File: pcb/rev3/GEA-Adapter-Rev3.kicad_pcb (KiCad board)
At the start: 2 copper layers, 88.7 x 40 mm, 109 parts, among them J1 8P8C, J3 TC2030, J4 USB_C_Receptacle_USB2.0_16P, Q3 CJ3407, Q4 CJ3407, Q5 MMBT3904, SW1 SW_Push, SW2 SW_Push, U10 TPS22810DBVR, U2 ESP32-C3-WROOM-02, U4 74LVC2G07, U5 74LVC2G07_3v3, U6 AP2112K-3.3, U7 USBLC6-2SC6, U8 AP63205WU, U9 TPS22810DBVR

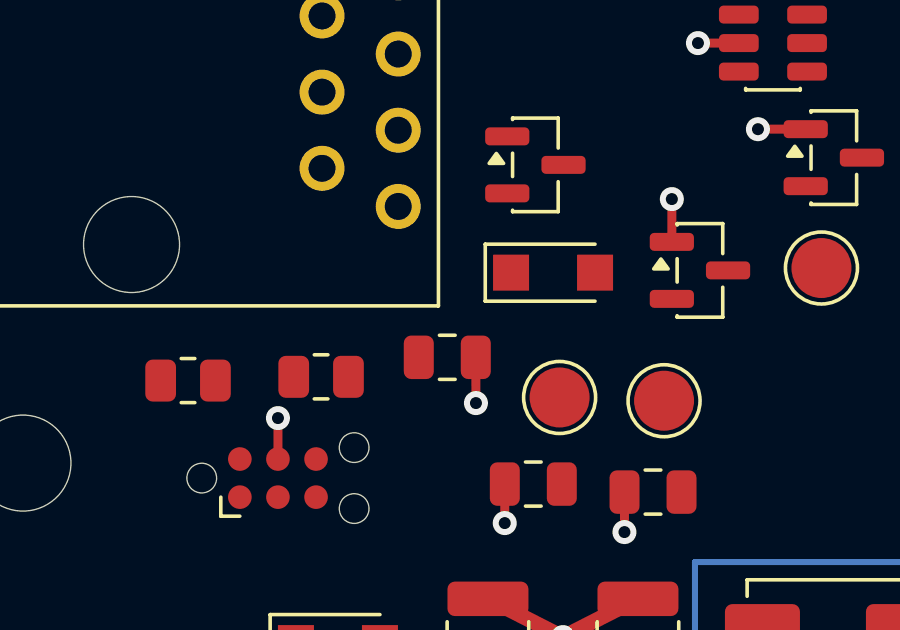
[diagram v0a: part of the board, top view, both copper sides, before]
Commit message: feat(pcb): route rev3a 5v branch
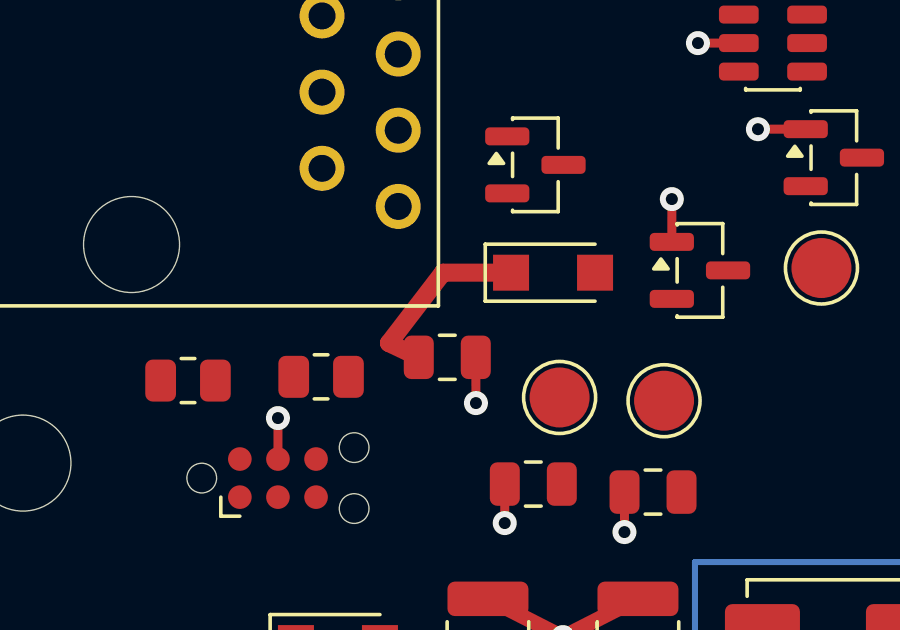
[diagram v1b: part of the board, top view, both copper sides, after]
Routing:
- net +5V: track 0.00 -> 6.33 mm
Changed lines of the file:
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@@
+	)
+	(segment
+		(start 20.270282 23.653262)
+		(end 18 23.653262)
+		(width 0.6)
+		(layer "F.Cu")
+		(net 2)
+	)
+	(segment
+		(start 18 23.653262)
+		(end 16.2 26)
+		(width 0.6)
+		(layer "F.Cu")
+		(net 2)
+	)
+	(segment
+		(start 16.2 26)
+		(end 17.194716 26.474524)
+		(width 0.6)
+		(layer "F.Cu")
+		(net 2)
 	)
 	(segment

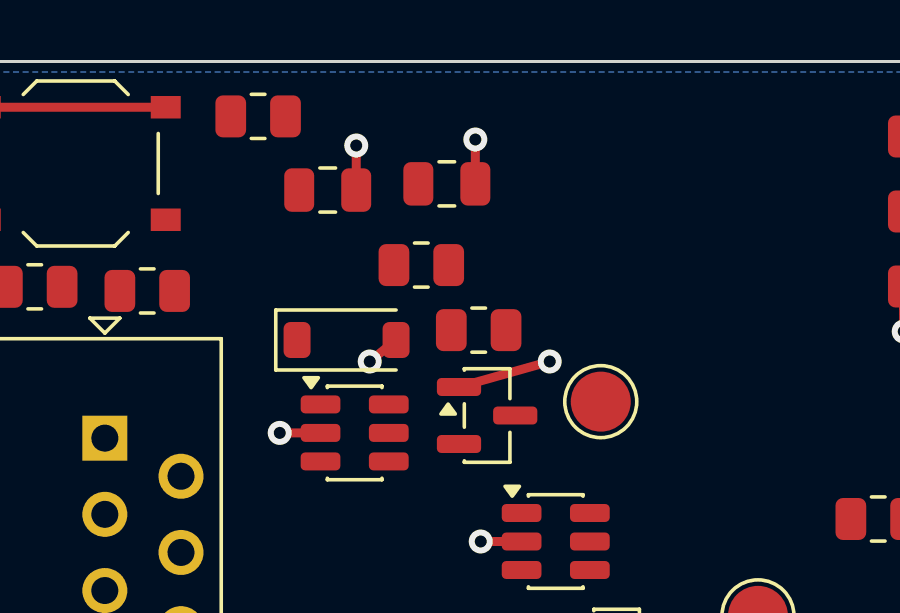
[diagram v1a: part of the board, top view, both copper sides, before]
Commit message: feat(pcb): route rev3a 3v3 branch
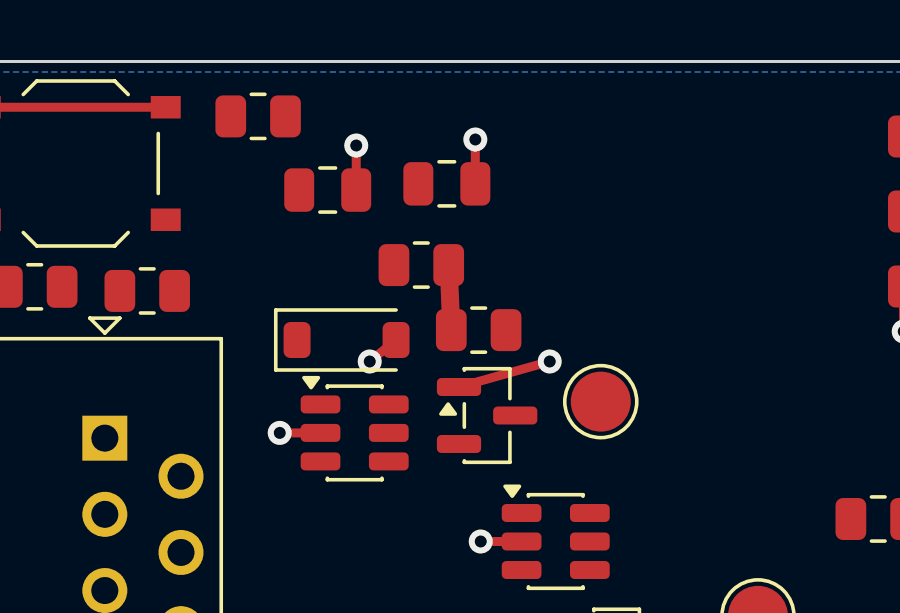
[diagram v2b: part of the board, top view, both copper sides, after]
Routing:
- net +3V3: track 0.00 -> 2.17 mm
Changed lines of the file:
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@@
+	)
+	(segment
+		(start 25.431711 6.786079)
+		(end 25.519272 8.9541)
+		(width 0.6)
+		(layer "F.Cu")
+		(net 1)
 	)
 	(segment

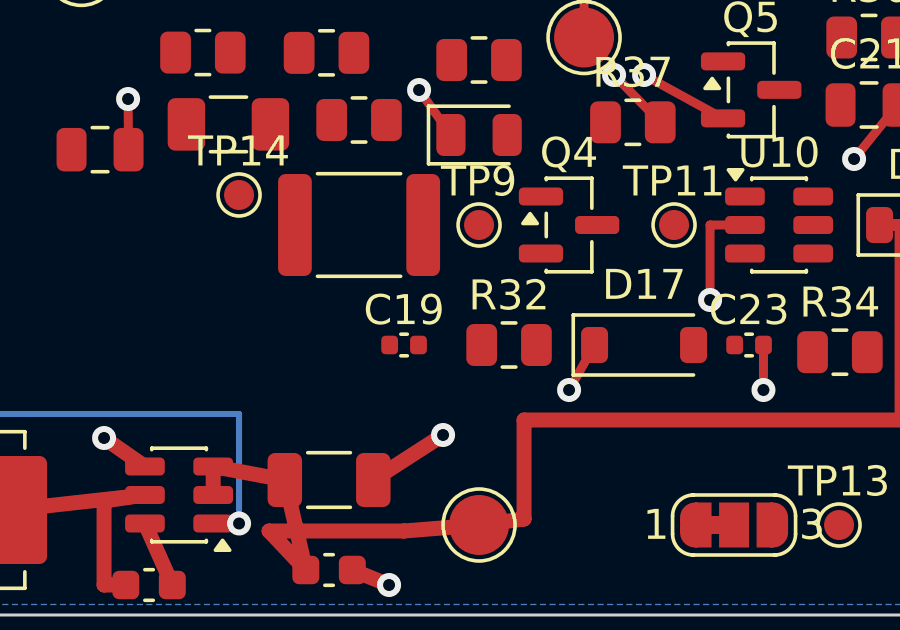
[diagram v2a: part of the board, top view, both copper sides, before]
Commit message: feat(pcb): route rev3a pin3 fused path
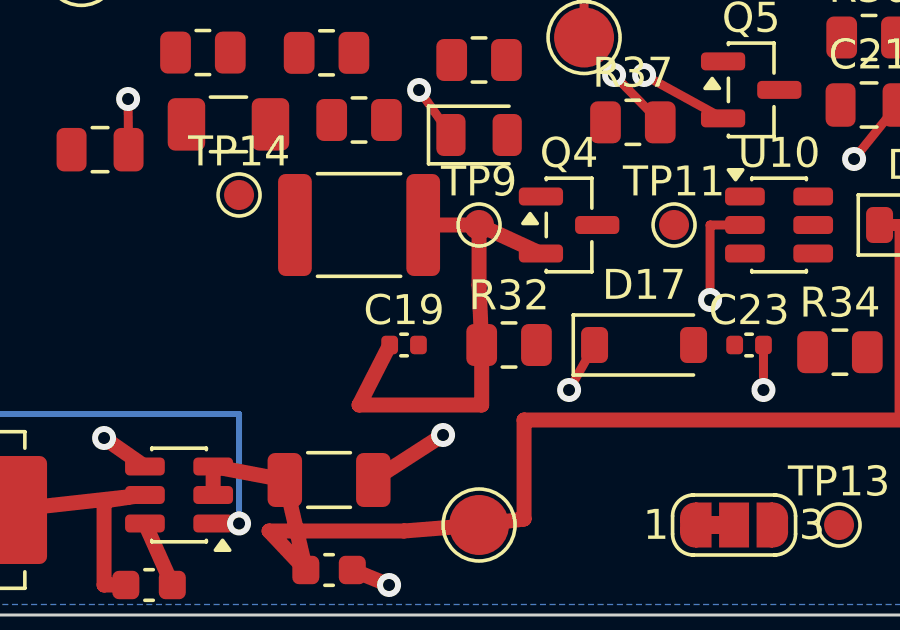
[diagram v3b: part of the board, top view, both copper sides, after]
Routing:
- net PIN3_FUSED: track 0.00 -> 16.5 mm
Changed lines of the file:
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@@
+	)
+	(segment
+		(start 47.1375 27)
+		(end 49 27)
+		(width 0.5)
+		(layer "F.Cu")
+		(net 58)
+	)
+	(segment
+		(start 49.0875 33)
+		(end 49.0875 31)
+		(width 0.5)
+		(layer "F.Cu")
+		(net 58)
+	)
+	(segment
+		(start 46.02 31)
+		(end 45 33)
+		(width 0.5)
+		(layer "F.Cu")
+		(net 58)
+	)
+	(segment
+		(start 49 27)
+		(end 51.0625 27.95)
+		(width 0.5)
+		(layer "F.Cu")
+		(net 58)
+	)
+	(segment
+		(start 45 33)
+		(end 49.0875 33)
+		(width 0.5)
+		(layer "F.Cu")
+		(net 58)
+	)
+	(segment
+		(start 49.0875 31)
+		(end 49 29)
+		(width 0.5)
+		(layer "F.Cu")
+		(net 58)
+	)
+	(segment
+		(start 49 29)
+		(end 49 27)
+		(width 0.5)
+		(layer "F.Cu")
+		(net 58)
 	)
 	(segment

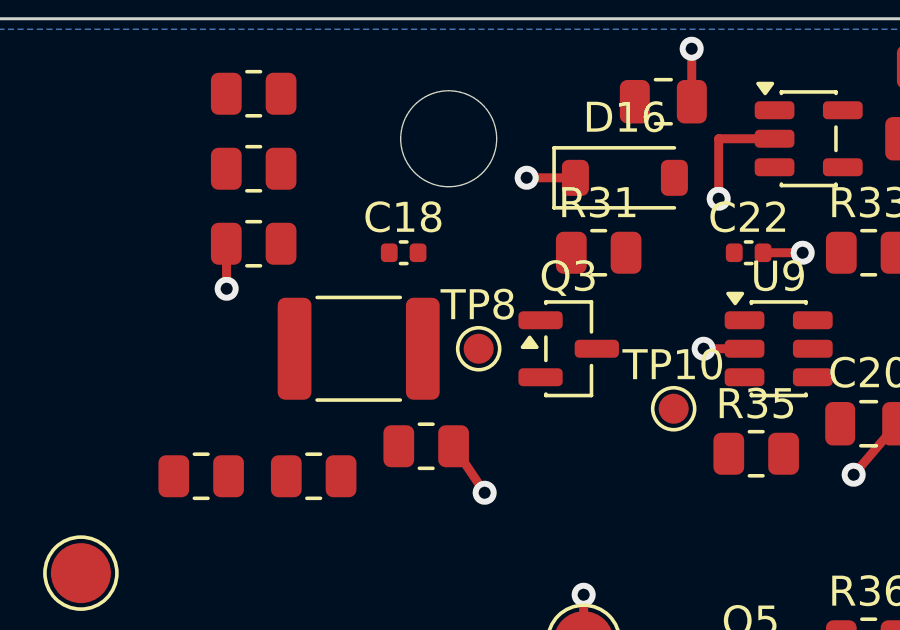
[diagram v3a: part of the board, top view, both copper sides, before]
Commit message: feat(pcb): route rev3a pin1 fused path
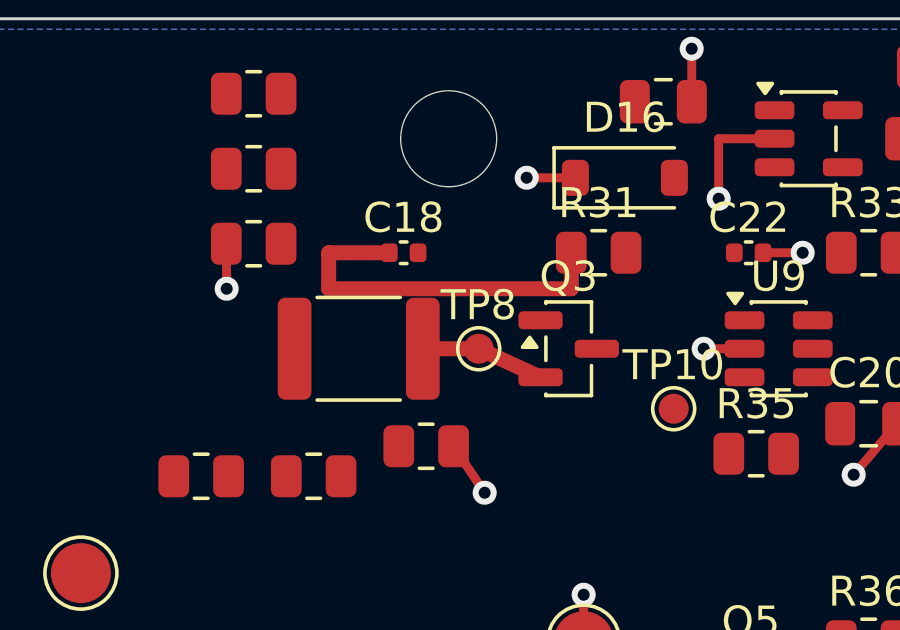
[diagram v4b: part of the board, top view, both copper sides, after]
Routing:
- net PIN1_FUSED: track 0.00 -> 16.6 mm
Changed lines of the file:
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@@
+	)
+	(segment
+		(start 46.02 7.8)
+		(end 44 7.8)
+		(width 0.5)
+		(layer "F.Cu")
+		(net 45)
+	)
+	(segment
+		(start 44 9)
+		(end 52.0875 9)
+		(width 0.5)
+		(layer "F.Cu")
+		(net 45)
+	)
+	(segment
+		(start 44 7.8)
+		(end 44 9)
+		(width 0.5)
+		(layer "F.Cu")
+		(net 45)
+	)
+	(segment
+		(start 52.0875 9)
+		(end 52.0875 7.8)
+		(width 0.5)
+		(layer "F.Cu")
+		(net 45)
+	)
+	(segment
+		(start 47.1375 11)
+		(end 49 11)
+		(width 0.5)
+		(layer "F.Cu")
+		(net 45)
+	)
+	(segment
+		(start 49 11)
+		(end 51.0625 11.95)
+		(width 0.5)
+		(layer "F.Cu")
+		(net 45)
 	)
 	(segment

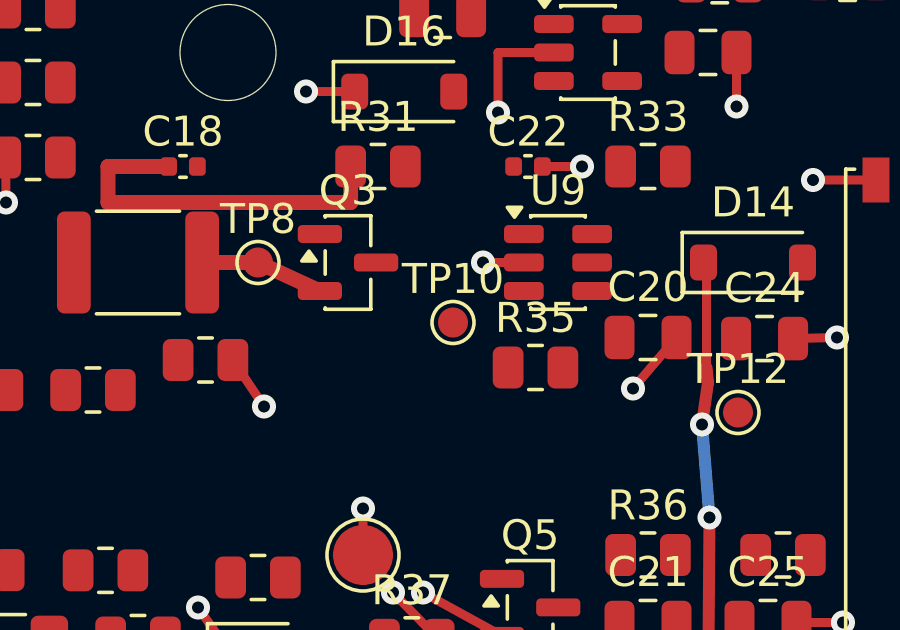
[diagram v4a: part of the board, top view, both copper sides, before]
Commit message: feat(pcb): route rev3a pin1 protected path
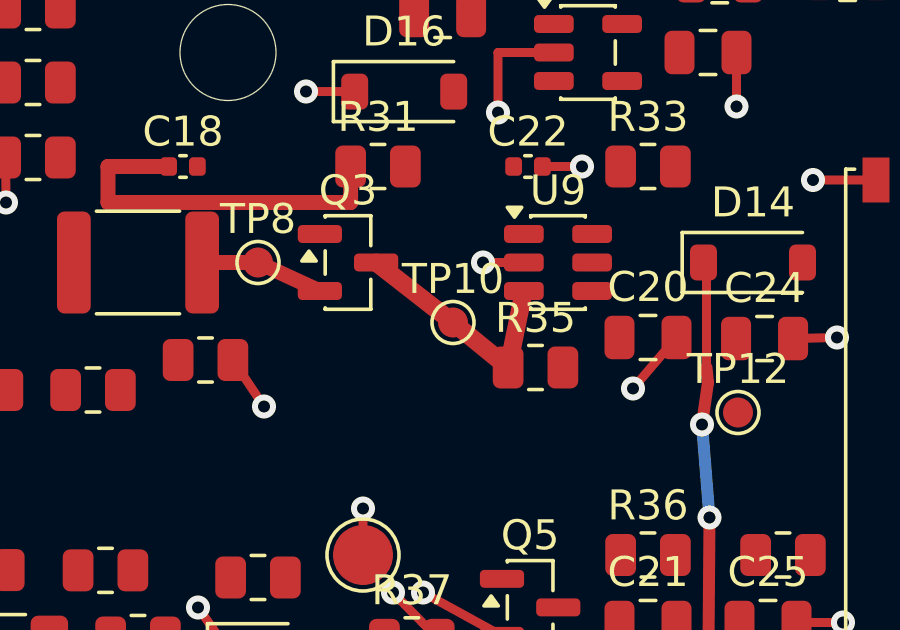
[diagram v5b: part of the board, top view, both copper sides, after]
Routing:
- net PIN1_PROTECTED: track 0.00 -> 8.23 mm
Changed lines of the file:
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@@
+	)
+	(segment
+		(start 52.9375 11)
+		(end 55.5 13)
+		(width 0.6)
+		(layer "F.Cu")
+		(net 42)
+	)
+	(segment
+		(start 57.8625 11.95)
+		(end 57.3375 14.5)
+		(width 0.6)
+		(layer "F.Cu")
+		(net 42)
+	)
+	(segment
+		(start 55.5 13)
+		(end 57.3375 14.5)
+		(width 0.6)
+		(layer "F.Cu")
+		(net 42)
 	)
 	(segment

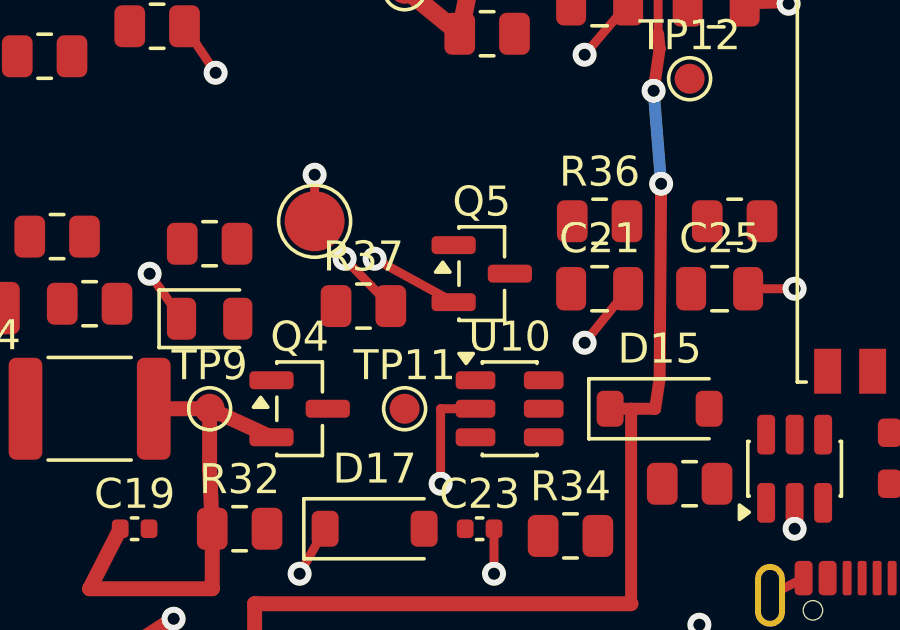
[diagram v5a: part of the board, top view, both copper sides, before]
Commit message: feat(pcb): route rev3a pin3 protected path
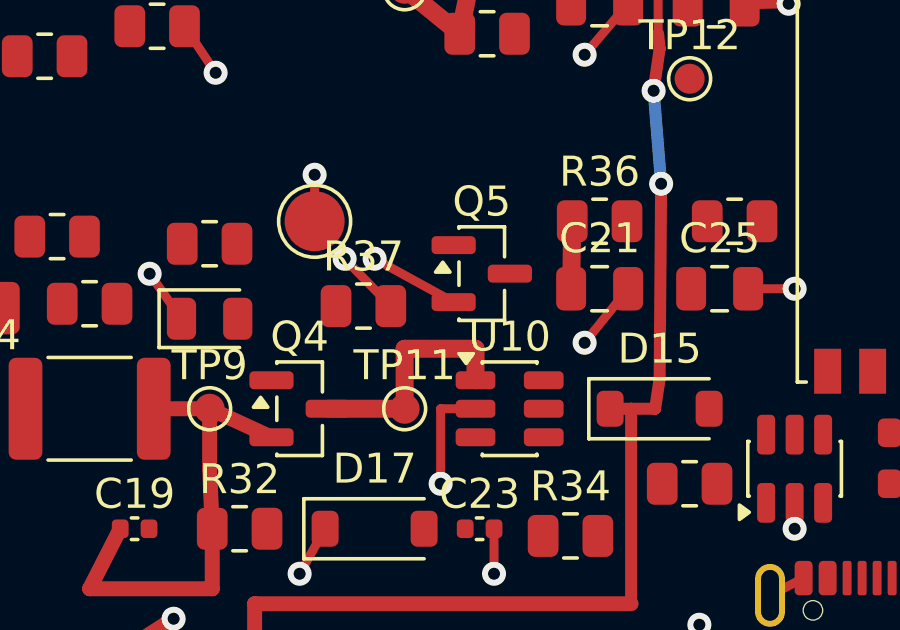
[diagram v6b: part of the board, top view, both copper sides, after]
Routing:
- net PIN3_PROTECTED: track 0.00 -> 10.2 mm
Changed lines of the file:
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@@
+	)
+	(segment
+		(start 61.0875 20.75)
+		(end 61.05 23)
+		(width 0.6)
+		(layer "F.Cu")
+		(net 59)
+	)
+	(segment
+		(start 55.5 27)
+		(end 55.5 25)
+		(width 0.6)
+		(layer "F.Cu")
+		(net 59)
+	)
+	(segment
+		(start 52.9375 27)
+		(end 55.5 27)
+		(width 0.6)
+		(layer "F.Cu")
+		(net 59)
+	)
+	(segment
+		(start 57.8625 25)
+		(end 57.8625 26.05)
+		(width 0.6)
+		(layer "F.Cu")
+		(net 59)
+	)
+	(segment
+		(start 55.5 25)
+		(end 57.8625 25)
+		(width 0.6)
+		(layer "F.Cu")
+		(net 59)
 	)
 	(segment

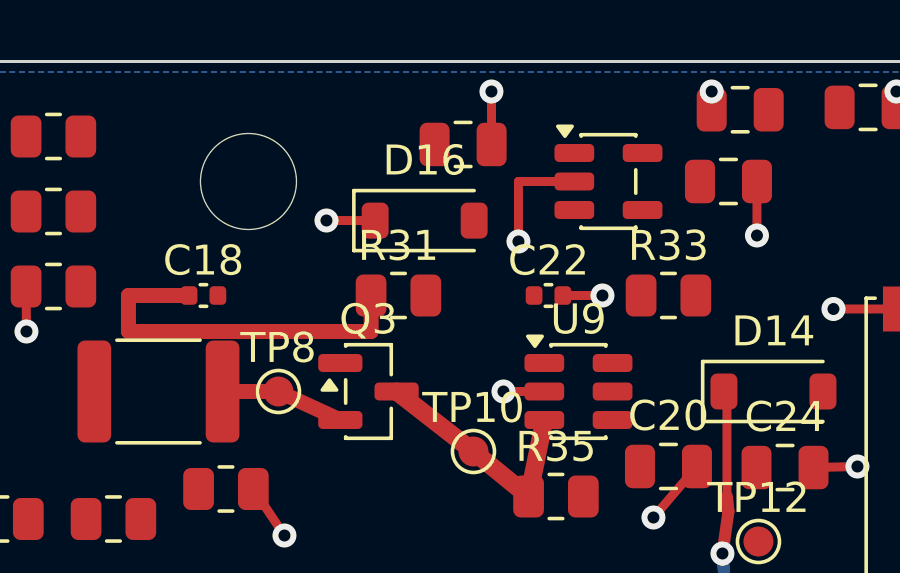
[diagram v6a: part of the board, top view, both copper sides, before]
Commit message: feat(pcb): route rev3a pin1 gate clamp
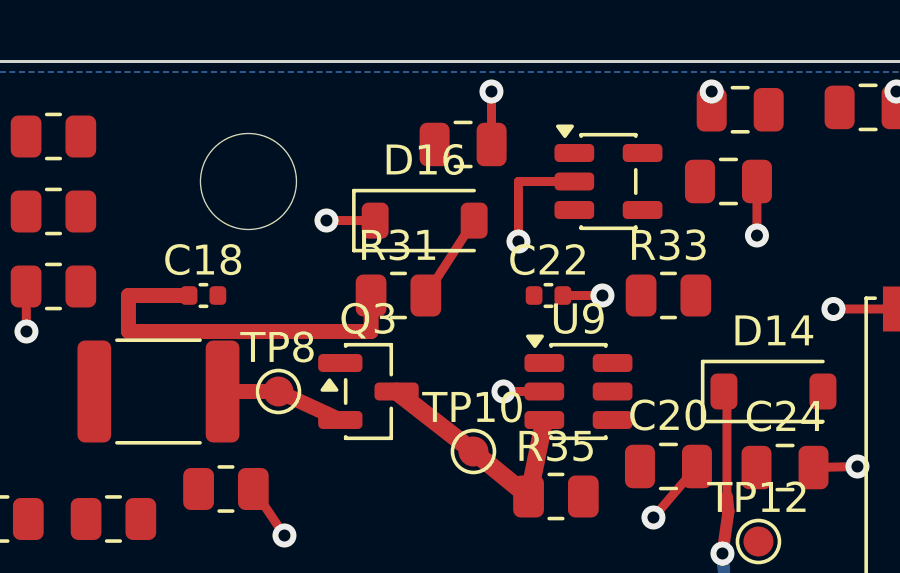
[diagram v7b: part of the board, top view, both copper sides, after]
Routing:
- net PIN1_GATE_CLAMP: track 0.00 -> 2.97 mm
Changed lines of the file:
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@@
+	)
+	(segment
+		(start 55.523377 5.303209)
+		(end 53.9125 7.8)
+		(width 0.3)
+		(layer "F.Cu")
+		(net 54)
 	)
 	(segment

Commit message: feat(pcb): route rev3a USB data path
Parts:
- moved U7 0.40 mm to (68.9, 29.0), turned to 0 degrees
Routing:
- net USB_CONN_N: track 0.00 -> 23.7 mm, vias 0 -> 2
- net USB_CONN_P: track 0.00 -> 23.3 mm, vias 0 -> 2
- net GND: track 94.1 -> 97.9 mm
- net USB_PROTECTED_P: track 0.00 -> 1.70 mm
- net USB_PROTECTED_N: track 0.00 -> 1.66 mm
